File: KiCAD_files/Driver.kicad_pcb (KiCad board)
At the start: 2 copper layers, 90 x 40 mm, 37 parts, among them J1 Driver_stage_outline_outputs, J2 Driver_stage_outline_inputs, U12 SFH617A-2X009T, U3 UCC21520DW, U4 UCC21520DW

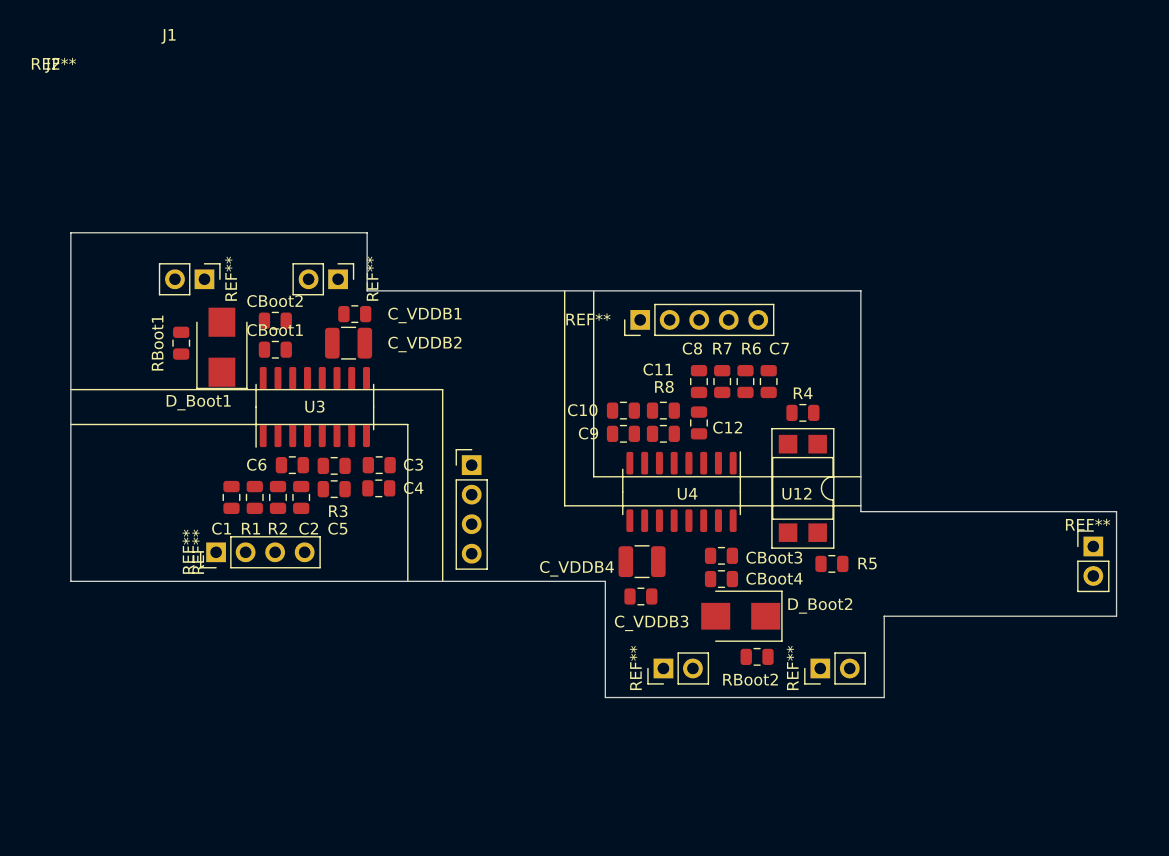
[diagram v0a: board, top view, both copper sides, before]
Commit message: Preliminary routing done - inter layers connectors issues to be solved
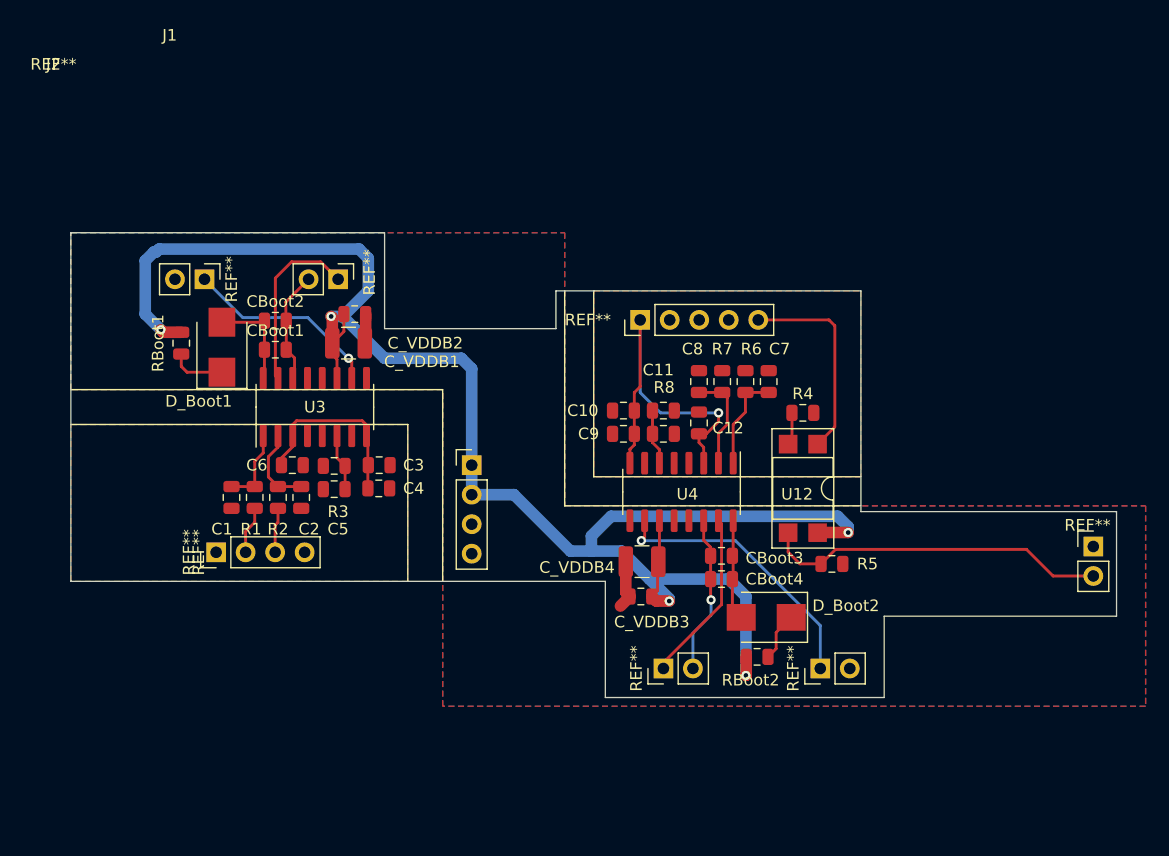
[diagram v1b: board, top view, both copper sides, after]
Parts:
- moved D_Boot2 2.20 mm to (88.8, 144.1)
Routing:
- net +15V: track 0.00 -> 141.8 mm, vias 0 -> 5
- net +5C: track 0.00 -> 48.0 mm, vias 0 -> 1
- net /Neutral_GND_cmd: track 0.00 -> 29.8 mm
- net /PWM_L2: track 0.00 -> 24.0 mm, vias 0 -> 1
- net /N_GND_cmd: track 0.00 -> 17.6 mm
- net /PWM_L1: track 0.00 -> 17.1 mm, vias 0 -> 1
- net /PWM_H1: track 0.00 -> 15.3 mm
- net /PWM_H2: track 0.00 -> 14.9 mm
- net /SW_Node2: track 0.00 -> 13.6 mm, vias 0 -> 1
- net /SW_Node1: track 0.00 -> 9.71 mm
- net Net-(CBoot1-Pad1): track 0.00 -> 8.72 mm
- net Net-(C8-Pad1): track 0.00 -> 8.59 mm
- net Net-(C7-Pad2): track 0.00 -> 8.52 mm
- net Net-(CBoot3-Pad1): track 0.00 -> 8.25 mm
- net Net-(C2-Pad1): track 0.00 -> 7.05 mm
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- added copper zone on F.Cu, net GNDD
- added copper zone on B.Cu, net GNDREF
- added copper zone on F.Cu, net GNDREF
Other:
- outline, holes or cut-outs redrawn

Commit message: Improved power board traces - Took a power electronic routing guideline into consideration.
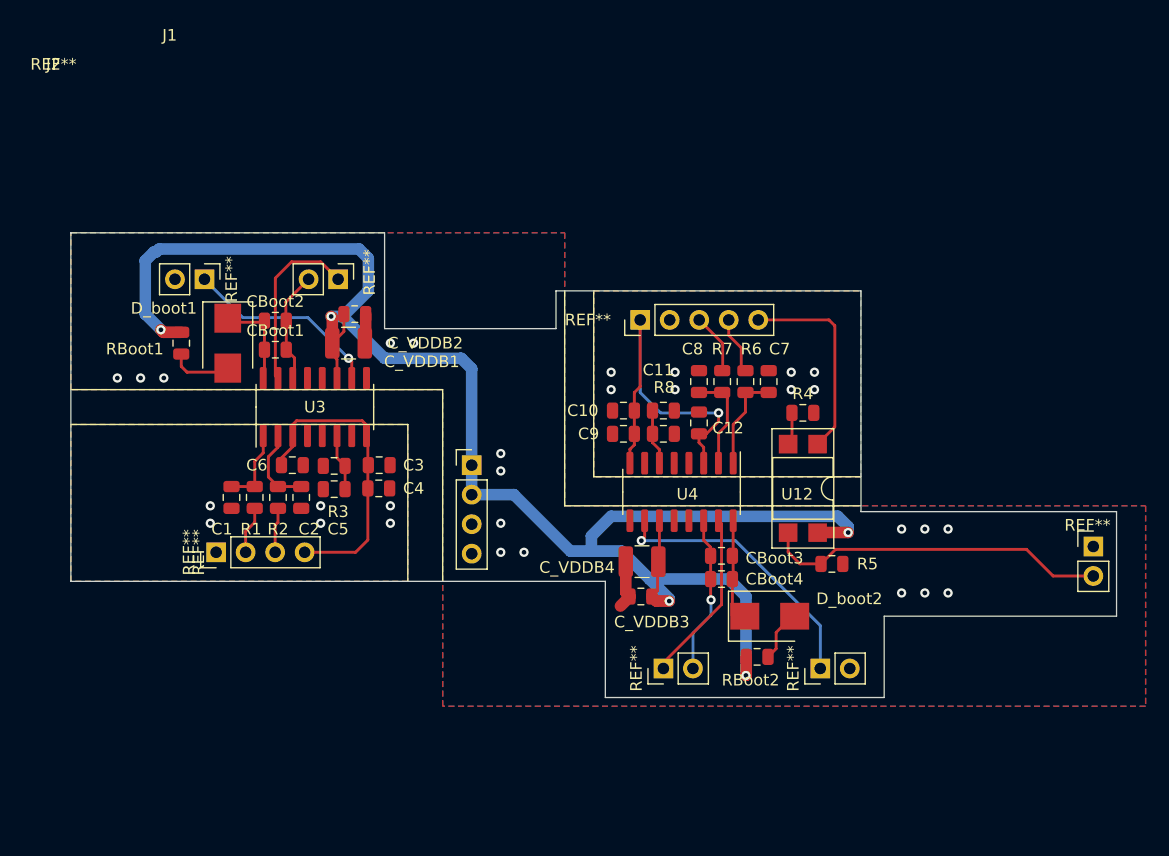
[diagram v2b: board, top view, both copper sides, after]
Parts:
- removed D_Boot1, D_Boot2: D_Schottky_AKA, Diode_SMD:D_SMB
- added D_boot1: D_Schottky, Diode_SMD:D_SMB, F.Cu at (42.5, 120.5)
- added D_boot2: D_Schottky, Diode_SMD:D_SMB, F.Cu at (89.2, 144.0)
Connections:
- net +5C renamed +5VD
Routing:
- net +5VD: track 48.0 -> 58.4 mm
- net /PWM_L2_D: track 0.00 -> 5.22 mm
- net /PWM_H2_D: track 0.00 -> 4.96 mm
- net GNDREF: vias 0 -> 16
- net GNDD: vias 0 -> 14
- added copper zone on B.Cu, net GNDD

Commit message: Added optional film caps - Added Heatsink mounting holes Verified mezzanine electrical connexions.
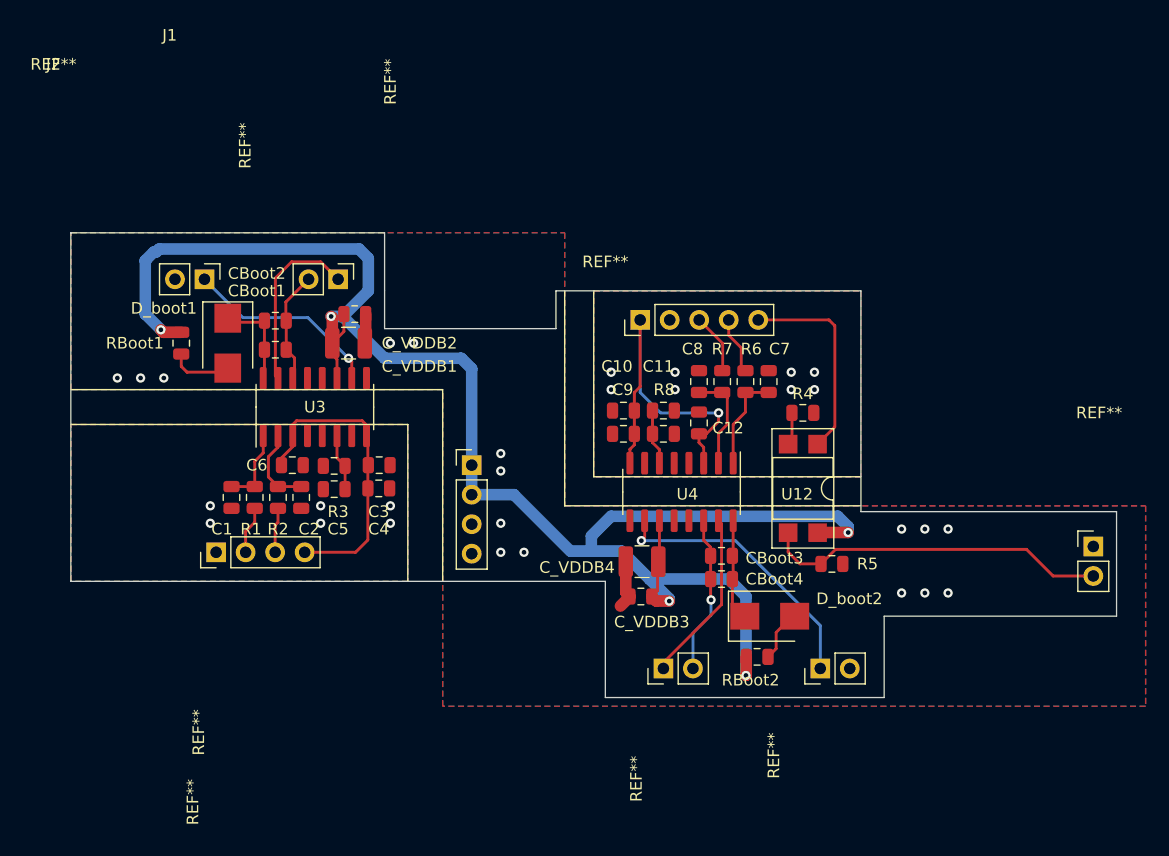
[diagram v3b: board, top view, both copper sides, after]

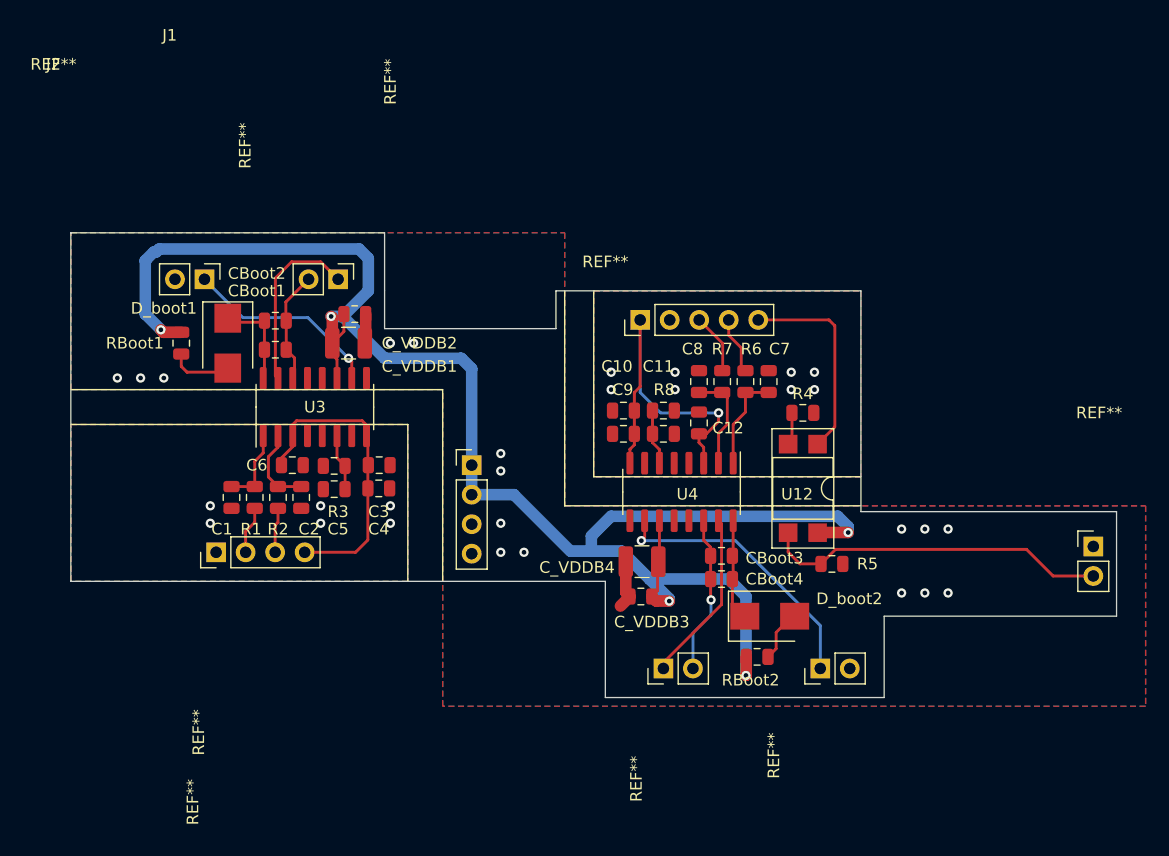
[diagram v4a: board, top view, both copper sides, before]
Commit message: Finalized BOM - Added mezzanine connectors overlay - Improved Nucleo shield
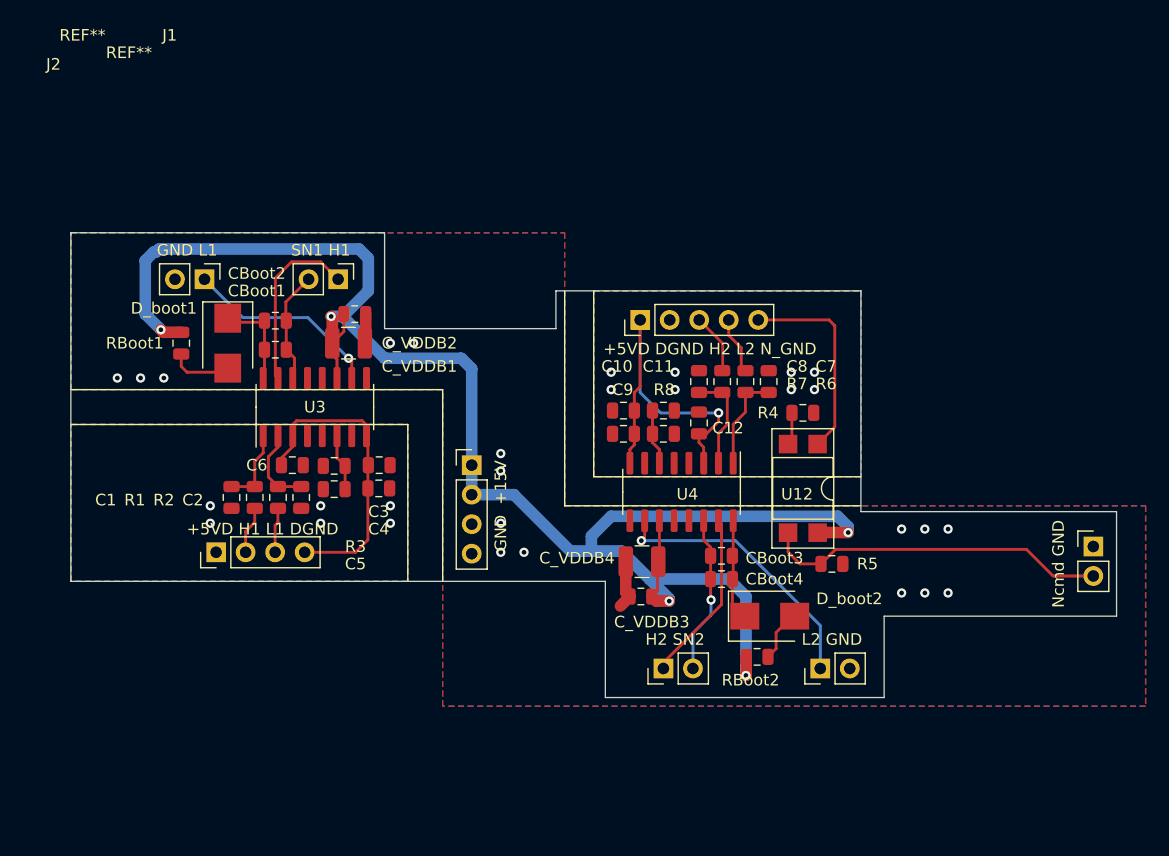
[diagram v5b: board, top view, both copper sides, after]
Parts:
- J1: value Driver_stage_outline_outputs -> Board outline
- J2: value Driver_stage_outline_inputs -> Driver_stage_outline

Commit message: Finalized overlay and added License info and current version Finalized the nucleo shield - added a CR2032 battery holder for the RTC.
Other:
- board text added: "CERN-OHL-S License"
- board text added: "Design J.Alinei"
- board text added: "Propulsed by OwnTech team under"
- board text added: "V1.0"

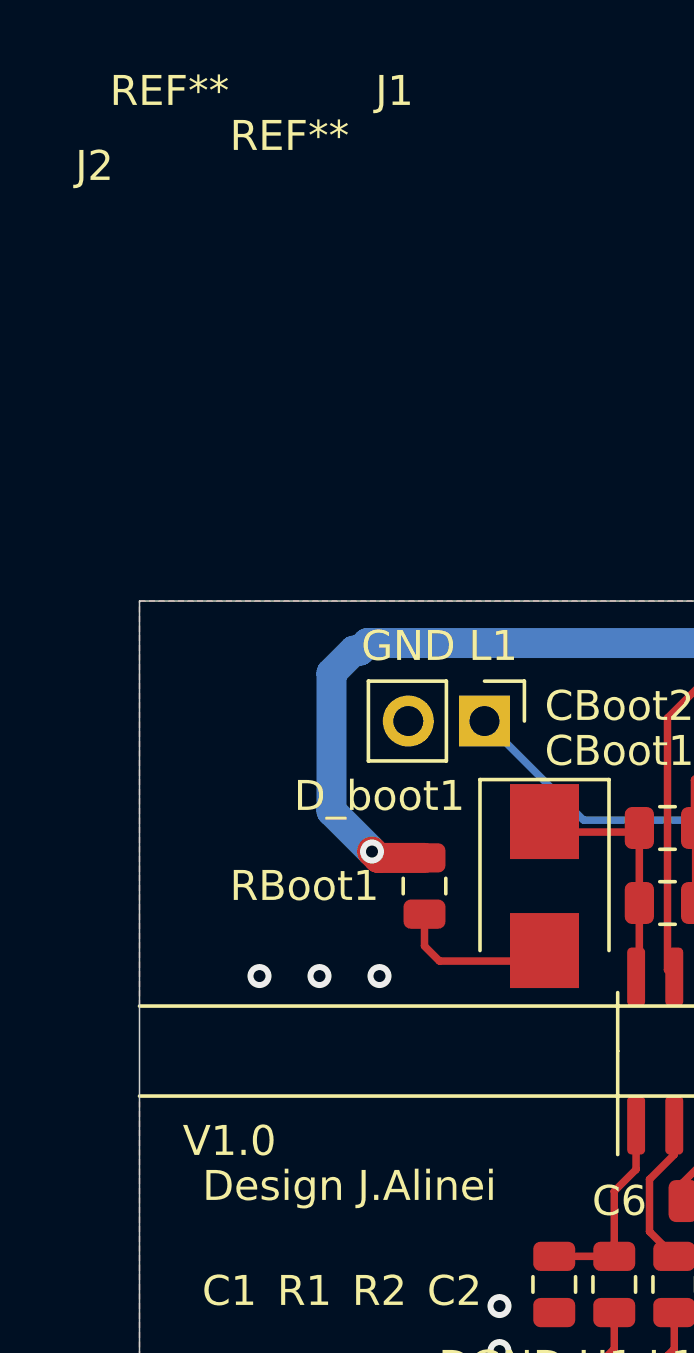
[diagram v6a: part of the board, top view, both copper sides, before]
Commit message: Solved minor glitch on the overlay.
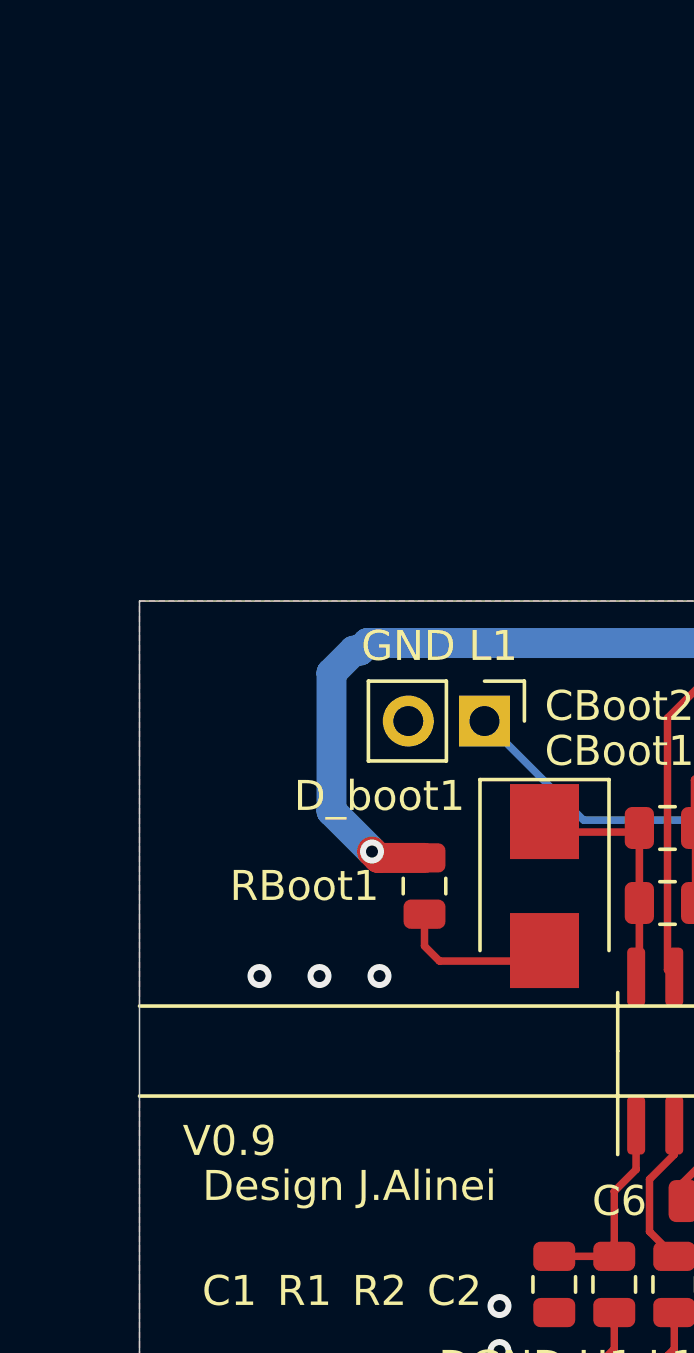
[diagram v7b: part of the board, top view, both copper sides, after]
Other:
- board text added: "V0.9"
- board text removed: "V1.0"

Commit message: Updated values in pcbnew - regenerated interactive BOM
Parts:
- C1, C10, C2, C4, C7, C8: value C_Small -> 33pF
- C12, C3, C6, C9: value C_Small -> 100nF
- CBoot2, CBoot4: value 1uF -> 100nF
- C_VDDB2, C_VDDB4: value 100nF -> 10uF
- D_boot1, D_boot2: value D_Schottky -> STTH4R02U
- J1: value Board outline -> Driver_stage_outline_outputs
- J2: value Driver_stage_outline -> Driver_stage_outline_inputs
- R1, R2, R4, R6, R7: value R_Small -> 51
- R3, R8: value R_Small -> 20k
- R5: value R_Small -> 1k
- RBoot1, RBoot2: value R -> 2.2
- U3, U4: value UCC21520DW -> UCC21222DR
